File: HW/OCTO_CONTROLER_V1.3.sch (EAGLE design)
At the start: 64 parts, among them IC1 NTMD5838NL, IC2 NTMD5838NL, IC3 CXDM4060P, IC4 AOZ1284PI, IC5 NTMD5838NL, IC6 NTMD5838NL, J1 DC_POWER, Q1 DTC114EUA, Q2 CXDM4060P, Q3 DTC114EUA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

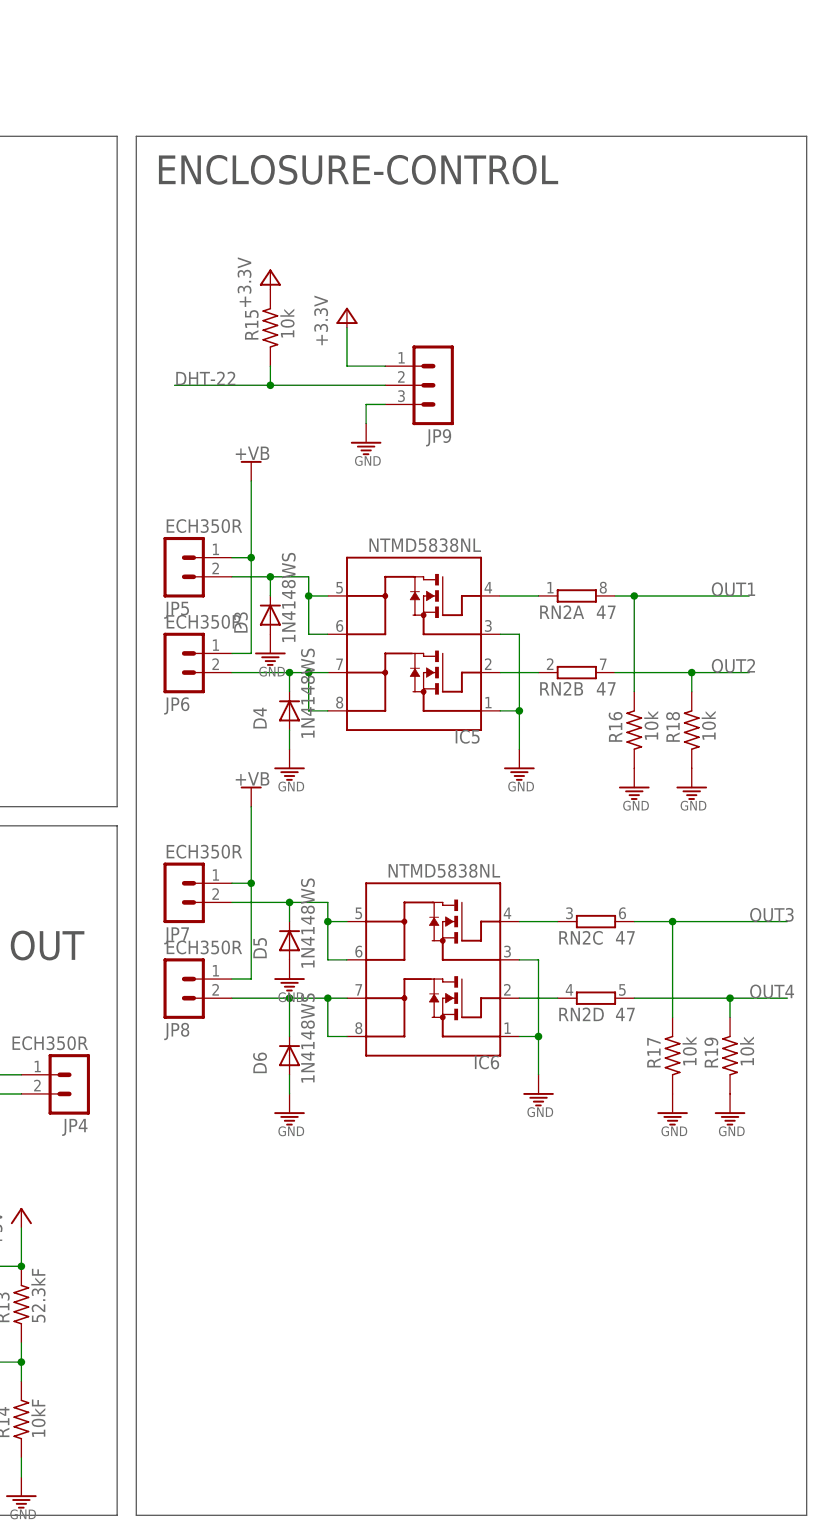
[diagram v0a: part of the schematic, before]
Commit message: V1.3 PCB PATHC
DHT-22 PULL-UP  10k->4.7K
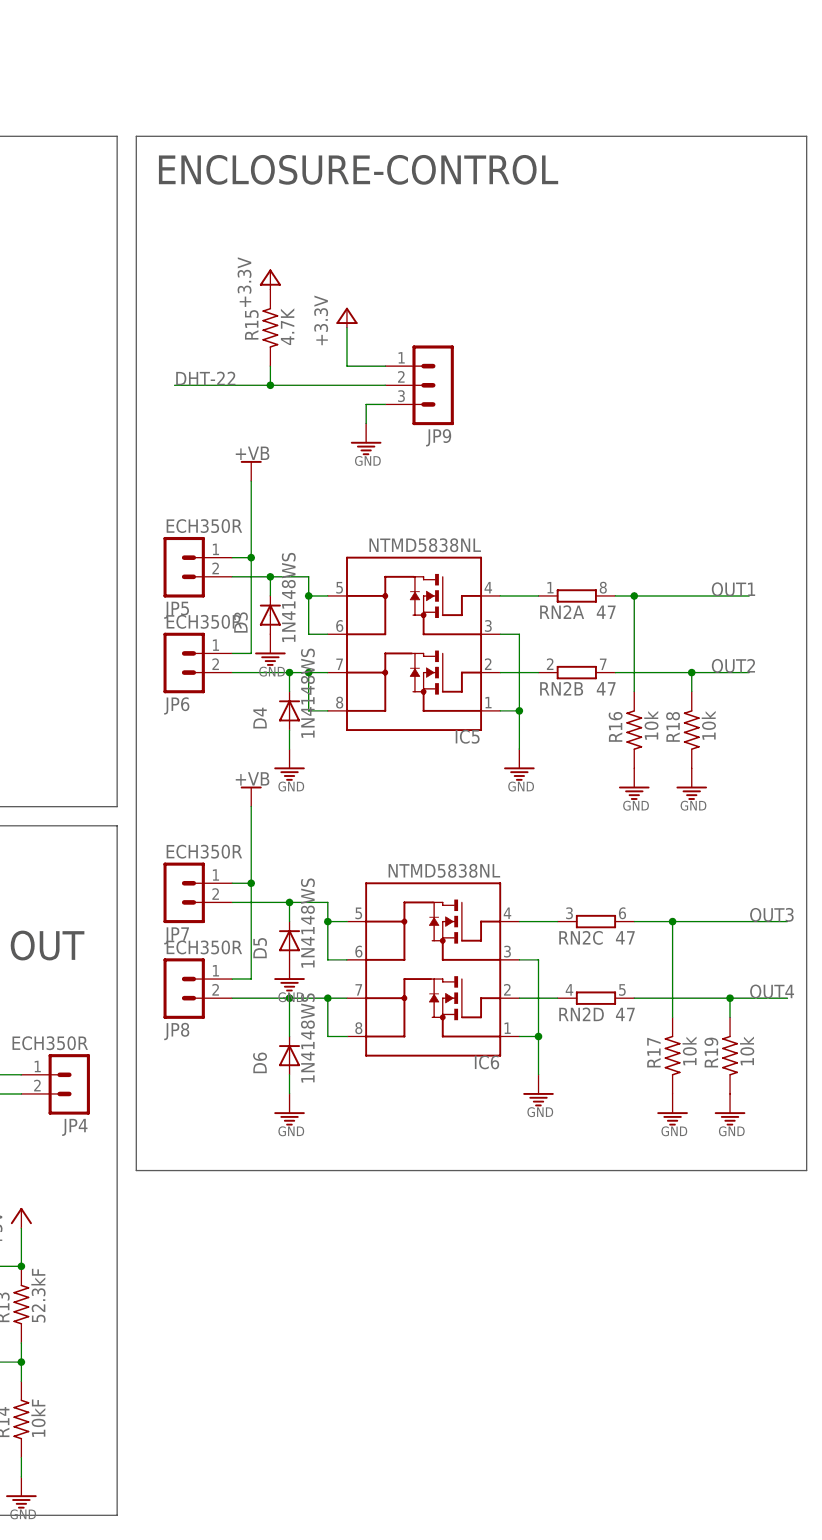
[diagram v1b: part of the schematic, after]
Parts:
- R15: value 10k -> 4.7K
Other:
- note added: "Output1/2"
- note added: "Output3/4"
- note removed: "Output1/2/3"
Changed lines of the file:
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@@
 <part name="PE25" library="cona_lib" deviceset="GND" device=""/>
 <part name="+3V4" library="cona_lib" deviceset="+3V3" device=""/>
-<part name="R15" library="cona_lib" deviceset="R_" device="0603" value="10k"/>
+<part name="R15" library="cona_lib" deviceset="R_" device="0603" value="4.7K"/>
 <part name="+3V5" library="cona_lib" deviceset="+3V3" device=""/>
 <part name="JP5" library="cona_lib" deviceset="MA02" device="ECH350R" value="ECH350R"/>
@@
 <text x="-127" y="-5.08" size="1.778" layer="98" rot="MR0">TP_CS</text>
 <text x="-172.72" y="-7.62" size="1.778" layer="98" rot="MR0">LCD_RS\</text>
-<wire x1="60.96" y1="-144.78" x2="60.96" y2="38.1" width="0.1524" layer="97"/>
+<wire x1="60.96" y1="-99.06" x2="60.96" y2="38.1" width="0.1524" layer="97"/>
 <wire x1="149.86" y1="38.1" x2="60.96" y2="38.1" width="0.1524" layer="97"/>
-<wire x1="149.86" y1="38.1" x2="149.86" y2="-144.78" width="0.1524" layer="97"/>
-<wire x1="149.86" y1="-144.78" x2="60.96" y2="-144.78" width="0.1524" layer="97"/>
+<wire x1="149.86" y1="38.1" x2="149.86" y2="-99.06" width="0.1524" layer="97"/>
+<wire x1="149.86" y1="-99.06" x2="60.96" y2="-99.06" width="0.1524" layer="97"/>
 <text x="63.5" y="35.56" size="3.81" layer="97" rot="MR180">ENCLOSURE-CONTROL</text>
 <text x="68.58" y="27.94" size="2.54" layer="98" rot="MR180">Temperature &amp; Humidity</text>
-<text x="83.82" y="-7.62" size="2.54" layer="98" rot="MR180">Output1/2/3</text>
-<text x="83.82" y="-50.8" size="2.54" layer="98" rot="MR180">Output1/2/3</text>
+<text x="91.44" y="-10.16" size="2.54" layer="98" rot="MR180">Output1/2</text>
+<text x="91.44" y="-53.34" size="2.54" layer="98" rot="MR180">Output3/4</text>
 </plain>
 <instances>
